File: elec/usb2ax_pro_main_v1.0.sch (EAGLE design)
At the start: 63 parts, among them J1 MICRO-USB-5P-340015001, J3 M10X2_SMD_1.27_FEMALE, K1 BUTTON-2P-REINFORCE-3100060P1, P1 PIN_SMD_2X2.5, P10 PIN_SMD_0.8X1.6, P11 PIN_SMD_0.8X1.6, P12 PIN_SMD_0.8X1.6, P13 PIN_SMD_1X2, P14 PIN_SMD_0.8X1.6, P15 PIN_SMD_0.8X1.6, P16 PIN_SMD_1X2, P2 PIN_SMD_2X2.5, P3 PIN_SMD_0.8X1.6, P4 PIN_SMD_0.8X1.6, P5 PIN_SMD_1X2, P6 PIN_SMD_1X2, P7 PIN_SMD_1X2, P8 PIN_SMD_1X2, P9 PIN_SMD_1X2, U1 ATSAM3U_C-AU, U2 MIC5205-3.3YM5, U3 BR24G256FJ-3AGTE2, U6 MPU-6050, X1 12MHz

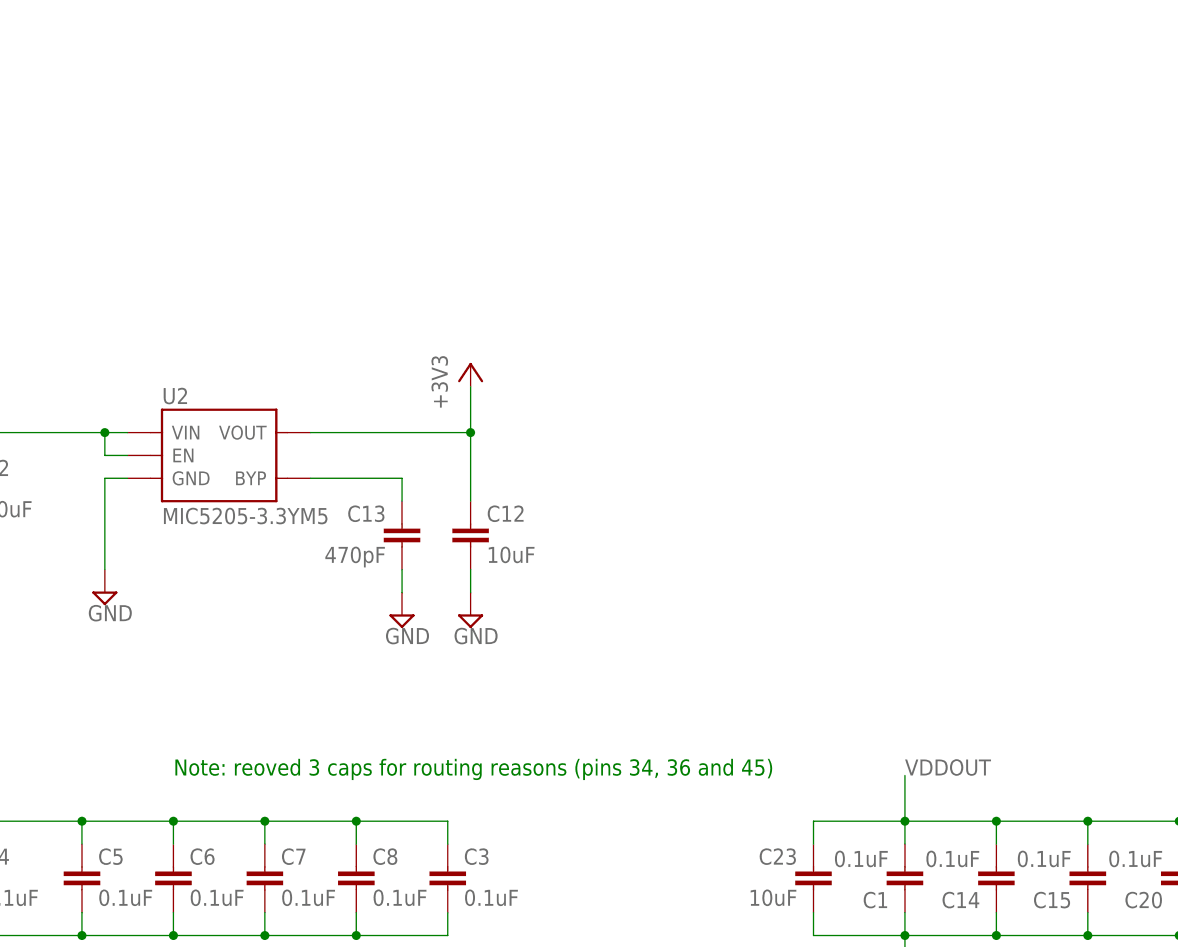
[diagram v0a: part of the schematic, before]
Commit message: Fixed 3V3 reg value
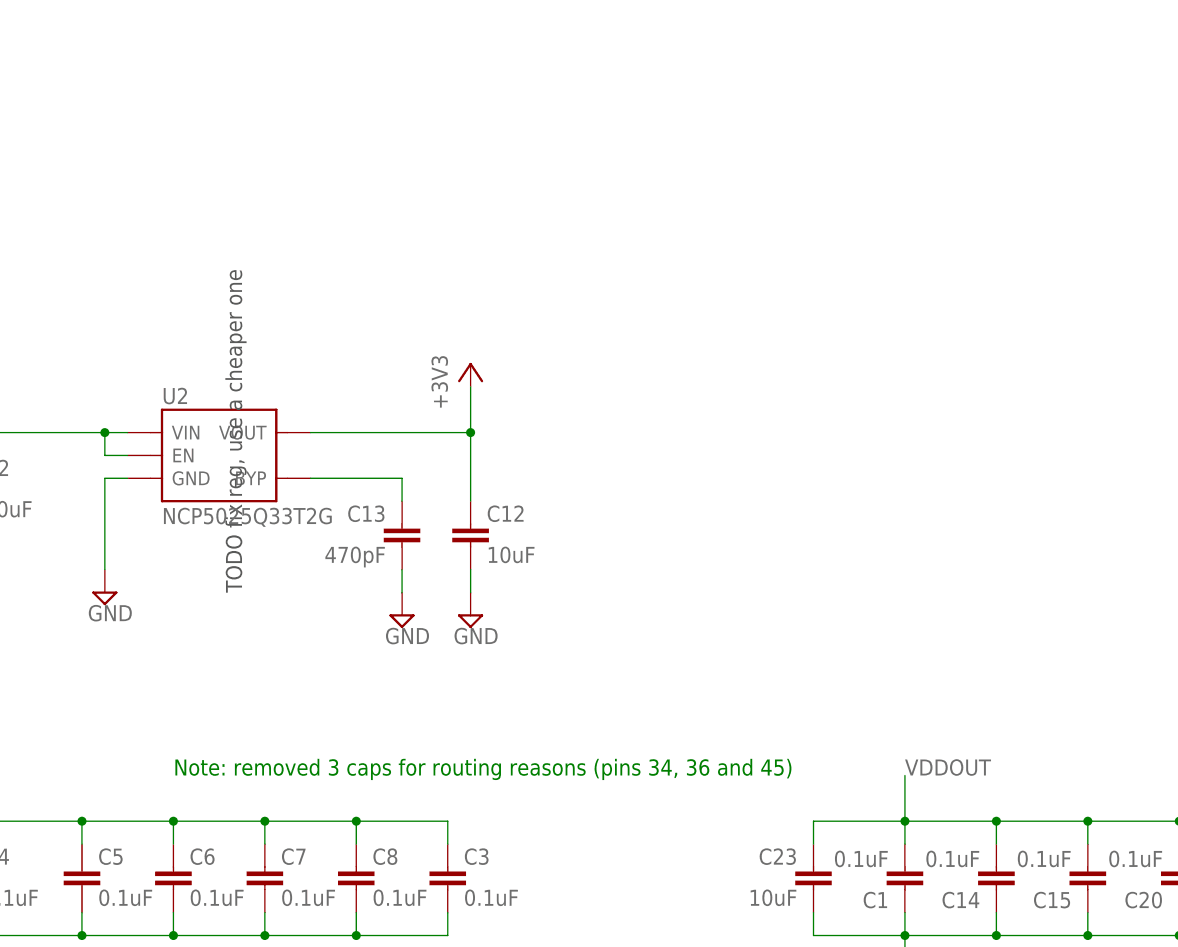
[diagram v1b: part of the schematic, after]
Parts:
- U2: value MIC5205-3.3YM5 -> NCP5025Q33T2G
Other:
- note added: "Note: removed 3 caps for routing reasons (pins 34, 36 and 45)"
- note added: "TODO fix reg, use a cheaper one"
- note removed: "Note: reoved 3 caps for routing reasons (pins 34, 36 and 45)"
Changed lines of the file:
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@@
 <grid distance="0.1" unitdist="inch" unit="inch" style="lines" multiple="1" display="no" altdistance="0.01" altunitdist="inch" altunit="inch"/>
 <layers>
-<layer number="1" name="Top" color="4" fill="1" visible="no" active="no"/>
-<layer number="2" name="Route2" color="1" fill="3" visible="no" active="no"/>
-<layer number="3" name="Route3" color="4" fill="3" visible="no" active="no"/>
-<layer number="14" name="Route14" color="1" fill="6" visible="no" active="no"/>
-<layer number="15" name="Route15" color="4" fill="6" visible="no" active="no"/>
-<layer number="16" name="Bottom" color="1" fill="1" visible="no" active="no"/>
-<layer number="17" name="Pads" color="2" fill="1" visible="no" active="no"/>
-<layer number="18" name="Vias" color="2" fill="1" visible="no" active="no"/>
-<layer number="19" name="Unrouted" color="6" fill="1" visible="no" active="no"/>
-<layer number="20" name="Dimension" color="15" fill="1" visible="no" active="no"/>
-<layer number="21" name="tPlace" color="7" fill="1" visible="no" active="no"/>
-<layer number="22" name="bPlace" color="7" fill="1" visible="no" active="no"/>
-<layer number="23" name="tOrigins" color="15" fill="1" visible="no" active="no"/>
-<layer number="24" name="bOrigins" color="15" fill="1" visible="no" active="no"/>
-<layer number="25" name="tNames" color="7" fill="1" visible="no" active="no"/>
-<layer number="26" name="bNames" color="7" fill="1" visible="no" active="no"/>
-<layer number="27" name="tValues" color="7" fill="1" visible="no" active="no"/>
-<layer number="28" name="bValues" color="7" fill="1" visible="no" active="no"/>
+<layer number="1" name="Top" color="4" fill="1" visible="yes" active="no"/>
+<layer number="2" name="Route2" color="1" fill="3" visible="yes" active="no"/>
+<layer number="3" name="Route3" color="4" fill="3" visible="yes" active="no"/>
+<layer number="14" name="Route14" color="1" fill="6" visible="yes" active="no"/>
+<layer number="15" name="Route15" color="4" fill="6" visible="yes" active="no"/>
+<layer number="16" name="Bottom" color="1" fill="1" visible="yes" active="no"/>
+<layer number="17" name="Pads" color="2" fill="1" visible="yes" active="no"/>
+<layer number="18" name="Vias" color="2" fill="1" visible="yes" active="no"/>
+<layer number="19" name="Unrouted" color="6" fill="1" visible="yes" active="no"/>
+<layer number="20" name="Dimension" color="15" fill="1" visible="yes" active="no"/>
+<layer number="21" name="tPlace" color="7" fill="1" visible="yes" active="no"/>
+<layer number="22" name="bPlace" color="7" fill="1" visible="yes" active="no"/>
+<layer number="23" name="tOrigins" color="15" fill="1" visible="yes" active="no"/>
+<layer number="24" name="bOrigins" color="15" fill="1" visible="yes" active="no"/>
+<layer number="25" name="tNames" color="7" fill="1" visible="yes" active="no"/>
+<layer number="26" name="bNames" color="7" fill="1" visible="yes" active="no"/>
+<layer number="27" name="tValues" color="7" fill="1" visible="yes" active="no"/>
+<layer number="28" name="bValues" color="7" fill="1" visible="yes" active="no"/>
 <layer number="29" name="tStop" color="7" fill="3" visible="no" active="no"/>
 <layer number="30" name="bStop" color="7" fill="6" visible="no" active="no"/>
@@
 <layer number="35" name="tGlue" color="7" fill="4" visible="no" active="no"/>
 <layer number="36" name="bGlue" color="7" fill="5" visible="no" active="no"/>
-<layer number="37" name="tTest" color="7" fill="1" visible="no" active="no"/>
-<layer number="38" name="bTest" color="7" fill="1" visible="no" active="no"/>
+<layer number="37" name="tTest" color="7" fill="1" visible="yes" active="no"/>
+<layer number="38" name="bTest" color="7" fill="1" visible="yes" active="no"/>
 <layer number="39" name="tKeepout" color="4" fill="11" visible="no" active="no"/>
 <layer number="40" name="bKeepout" color="1" fill="11" visible="no" active="no"/>
@@
 <layer number="44" name="Drills" color="7" fill="1" visible="no" active="no"/>
 <layer number="45" name="Holes" color="7" fill="1" visible="no" active="no"/>
-<layer number="46" name="Milling" color="3" fill="1" visible="no" active="no"/>
-<layer number="47" name="Measures" color="7" fill="1" visible="no" active="no"/>
-<layer number="48" name="Document" color="7" fill="1" visible="no" active="no"/>
-<layer number="49" name="Reference" color="7" fill="1" visible="no" active="no"/>
-<layer number="50" name="dxf" color="7" fill="1" visible="no" active="no"/>
-<layer number="51" name="tDocu" color="7" fill="1" visible="no" active="no"/>
-<layer number="52" name="bDocu" color="7" fill="1" visible="no" active="no"/>
-<layer number="53" name="tGND_GNDA" color="7" fill="9" visible="no" active="no"/>
-<layer number="54" name="bGND_GNDA" color="1" fill="9" visible="no" active="no"/>
-<layer number="56" name="wert" color="7" fill="1" visible="no" active="no"/>
+<layer number="46" name="Milling" color="3" fill="1" visible="yes" active="no"/>
+<layer number="47" name="Measures" color="7" fill="1" visible="yes" active="no"/>
+<layer number="48" name="Document" color="7" fill="1" visible="yes" active="no"/>
+<layer number="49" name="Reference" color="7" fill="1" visible="yes" active="no"/>
+<layer number="50" name="dxf" color="7" fill="1" visible="yes" active="no"/>
+<layer number="51" name="tDocu" color="7" fill="1" visible="yes" active="no"/>
+<layer number="52" name="bDocu" color="7" fill="1" visible="yes" active="no"/>
+<layer number="53" name="tGND_GNDA" color="7" fill="9" visible="yes" active="no"/>
+<layer number="54" name="bGND_GNDA" color="1" fill="9" visible="yes" active="no"/>
+<layer number="56" name="wert" color="7" fill="1" visible="yes" active="no"/>
 <layer number="90" name="Modules" color="5" fill="1" visible="yes" active="yes"/>
 <layer number="91" name="Nets" color="2" fill="1" visible="yes" active="yes"/>
@@
 <part name="X1" library="OPL" deviceset="CRYSTAL*" device="-0500290P1" value="12MHz"/>
 <part name="C12" library="Xevelabs" deviceset="C" device="0805" value="10uF"/>
-<part name="U2" library="OPL" deviceset="MIC5205-3.3YM5" device=""/>
+<part name="U2" library="OPL" deviceset="MIC5205-3.3YM5" device="" value="NCP5025Q33T2G"/>
 <part name="C13" library="Xevelabs" deviceset="C" device="0201" value="470pF"/>
 <part name="+3V8" library="supply1" deviceset="+3V3" device=""/>
@@
 <text x="223.774" y="62.738" size="1.778" layer="91">NC</text>
 <text x="378.46" y="83.82" size="1.778" layer="92" rot="R90">TODO protect ADC from reverse 12V ?</text>
-<text x="2.54" y="187.96" size="1.778" layer="91">Note: reoved 3 caps for routing reasons (pins 34, 36 and 45)</text>
+<text x="2.54" y="187.96" size="1.778" layer="91">Note: removed 3 caps for routing reasons (pins 34, 36 and 45)</text>
 <text x="149.86" y="157.48" size="1.27" layer="97">PWMH0
 PWMH1
@@
 <text x="152.4" y="109.22" size="1.27" layer="97">TWD1
 TWCK1</text>
+<text x="10.16" y="208.28" size="1.778" layer="92" rot="R90">TODO fix reg, use a cheaper one</text>
 </plain>
 <instances>
